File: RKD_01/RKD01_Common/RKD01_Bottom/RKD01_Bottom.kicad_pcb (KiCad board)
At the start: 2 copper layers, 209.5 x 126.2 mm, 10 parts, among them M1 Mark, M2 Mark, M3 Mark, M4 Mark, M5 Mark, M6 Mark, M7 Mark, M8 Mark, M9 Mark

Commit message: Bottomパーツの左右共通化
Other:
- board text added: "RKD01 v1.0"
- board text removed: "RKD01_Right v1.0"
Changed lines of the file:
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@@
 		(layer "F.Fab")
 	)
-	(gr_text "RKD01_Right v1.0"
+	(gr_text "RKD01 v1.0"
 		(at 214.3125 23.8125 0)
 		(layer "B.SilkS")

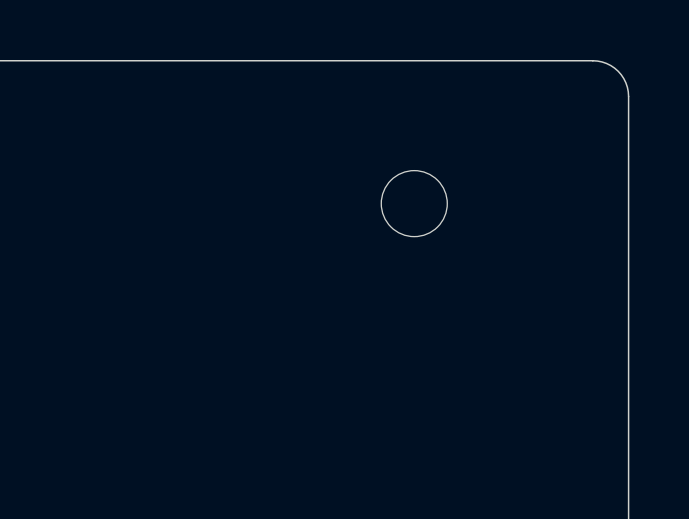
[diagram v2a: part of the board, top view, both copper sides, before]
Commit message: ネジ穴位置の誤り修正
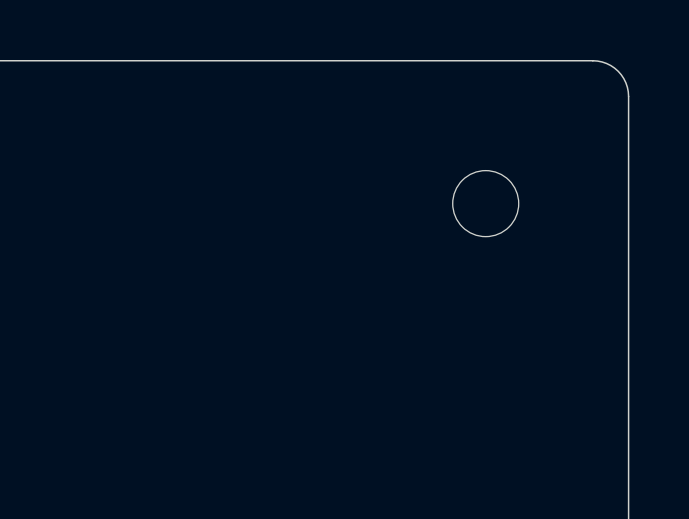
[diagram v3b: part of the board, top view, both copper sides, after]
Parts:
- moved M2 2.38 mm to (226.2, 23.8)
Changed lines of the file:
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@@
 	(footprint "kbd_Hole:m2_Screw_Hole"
 		(layer "F.Cu")
-		(at 223.8375 23.8125)
+		(at 226.21875 23.8125)
 		(descr "Mounting Hole 2.2mm, no annular, M2")
 		(tags "mounting hole 2.2mm no annular m2")

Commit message: ScrewHall追加
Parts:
- Point1: footprint Rikkodo_FootPrint:rkd_Point_Hall -> Rikkodo_FootPrint:rkd_Point_Screw_Hall
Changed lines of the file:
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@@
 		)
 	)
-	(footprint "Rikkodo_FootPrint:rkd_Point_Hall"
+	(footprint "Rikkodo_FootPrint:rkd_Point_Screw_Hall"
 		(layer "F.Cu")
 		(at 30.95625 101.203125)
@@
 			)
 		)
-		(property "Footprint" "Rikkodo_FootPrint:rkd_Point_Hall"
+		(property "Footprint" "Rikkodo_FootPrint:rkd_Point_Screw_Hall"
 			(at 0 0 0)
 			(layer "F.Fab")

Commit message: v1.5
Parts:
- added M10: Mark, kbd_Hole:m2_Screw_Hole, F.Cu at (164.3, 66.7)
- added M11: Mark, kbd_Hole:m2_Screw_Hole, F.Cu at (83.3, 104.8)
- added M12: Mark, kbd_Hole:m2_Screw_Hole, F.Cu at (178.6, 66.7)
- added M13: Mark, kbd_Hole:m2_Screw_Hole, F.Cu at (90.5, 104.8)
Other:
- board text added: "RKD01 v1.5"
- board text removed: "RKD01 v1.0"

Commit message: 配置変更
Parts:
- moved M13 26.2 mm to (116.7, 104.8)
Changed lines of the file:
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@@
 	(footprint "kbd_Hole:m2_Screw_Hole"
 		(layer "F.Cu")
-		(at 90.4875 104.775)
+		(at 116.68125 104.775)
 		(descr "Mounting Hole 2.2mm, no annular, M2")
 		(tags "mounting hole 2.2mm no annular m2")

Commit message: バージョン表記を修正
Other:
- board text added: "RKD01 v2"
- board text removed: "RKD01 v1.5"
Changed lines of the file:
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@@
 		(layer "F.Fab")
 	)
-	(gr_text "RKD01 v1.5"
+	(gr_text "RKD01 v2"
 		(at 214.3125 23.8125 0)
 		(layer "B.SilkS")
